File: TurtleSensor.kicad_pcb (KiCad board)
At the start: 2 copper layers, 40 x 40 mm, 14 parts, among them IC1 ATMEGA328P-A, J2 FTDIConnector, U1 SI7021, U2 M24512

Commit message: rotated capacitor to be parallel
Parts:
- moved 22pF2 0.90 mm to (135.0, 103.0), turned to 90 degrees
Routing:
- net Net-(22pF2-Pad2): track 10.5 -> 8.98 mm
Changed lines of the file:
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@@
     (thickness 1.6)
     (drawings 4)
-    (tracks 168)
+    (tracks 167)
     (zones 0)
     (modules 14)
@@
   )
   (module Capacitors_SMD:C_0805_HandSoldering placed (layer F.Cu)
-    (at 134.25 103.5 135)
+    (at 135 103 90)
     (descr "Capacitor SMD 0805, hand soldering")
     (tags "capacitor 0805")
     (attr smd)
-    (fp_text reference 22pF2 (at 0 -2.1 135) (layer F.SilkS)
-      (effects (font (size 1 1) (thickness 0.15)))
-    )
-    (fp_text value C (at 0 2.1 135) (layer F.Fab)
+    (fp_text reference 22pF2 (at 0 -2.1 90) (layer F.SilkS)
+      (effects (font (size 1 1) (thickness 0.15)))
+    )
+    (fp_text value C (at 0 2.1 90) (layer F.Fab)
       (effects (font (size 1 1) (thickness 0.15)))
     )
@@
     (fp_line (start 0.5 -0.85) (end -0.5 -0.85) (layer F.SilkS) (width 0.15))
     (fp_line (start -0.5 0.85) (end 0.5 0.85) (layer F.SilkS) (width 0.15))
-    (pad 1 smd rect (at -1.25 0 135) (size 1.5 1.25) (layers F.Cu F.Paste F.Mask)
-      (net 3 GND))
-    (pad 2 smd rect (at 1.25 0 135) (size 1.5 1.25) (layers F.Cu F.Paste F.Mask)
+    (pad 1 smd rect (at -1.25 0 90) (size 1.5 1.25) (layers F.Cu F.Paste F.Mask)
+      (net 3 GND))
+    (pad 2 smd rect (at 1.25 0 90) (size 1.5 1.25) (layers F.Cu F.Paste F.Mask)
       (net 2 "Net-(22pF2-Pad2)"))
     (model Capacitors_SMD.3dshapes/C_0805_HandSoldering.wrl
@@
     (effects (font (size 1.5 1.5) (thickness 0.3)))
   )
-  (segment (start 133 91.75) (end 133 93.65) (width 0.4) (layer F.Cu) (net 1) (status 400000))
-  (segment (start 133 93.65) (end 135 95.65) (width 0.4) (layer F.Cu) (net 1) (status 800000))
-  (segment (start 140.25 96.75) (end 136.75 96.75) (width 0.4) (layer F.Cu) (net 1) (status 400000))
-  (segment (start 136.75 96.75) (end 135.65 95.65) (width 0.4) (layer F.Cu) (net 1) (status 800000))
-  (segment (start 135.65 95.65) (end 135 95.65) (width 0.4) (layer F.Cu) (net 1) (status C00000))
-  (segment (start 135 95.65) (end 135 95) (width 0.3) (layer F.Cu) (net 1) (status C00000))
+  (segment (start 133 91.75) (end 133 93.65) (width 0.4) (layer F.Cu) (net 1))
+  (segment (start 133 93.65) (end 135 95.65) (width 0.4) (layer F.Cu) (net 1))
+  (segment (start 140.25 96.75) (end 136.75 96.75) (width 0.4) (layer F.Cu) (net 1))
+  (segment (start 136.75 96.75) (end 135.65 95.65) (width 0.4) (layer F.Cu) (net 1))
+  (segment (start 135.65 95.65) (end 135 95.65) (width 0.4) (layer F.Cu) (net 1))
+  (segment (start 135 95.65) (end 135 95) (width 0.3) (layer F.Cu) (net 1))
   (segment (start 133 92) (end 133 91.75) (width 0.25) (layer F.Cu) (net 1))
-  (segment (start 135 98.35) (end 135 100.982234) (width 0.4) (layer F.Cu) (net 2) (status 400000))
-  (segment (start 135 100.982234) (end 133.366117 102.616117) (width 0.4) (layer F.Cu) (net 2) (status 800000))
-  (segment (start 140.25 97.55) (end 137.45 97.55) (width 0.4) (layer F.Cu) (net 2) (status 400000))
-  (segment (start 136.65 98.35) (end 135 98.35) (width 0.4) (layer F.Cu) (net 2) (status 800000))
+  (segment (start 135 98.35) (end 135 101.75) (width 0.4) (layer F.Cu) (net 2) (status C00000))
+  (segment (start 140.25 97.55) (end 137.45 97.55) (width 0.4) (layer F.Cu) (net 2))
+  (segment (start 136.65 98.35) (end 135 98.35) (width 0.4) (layer F.Cu) (net 2))
   (segment (start 137.45 97.55) (end 136.65 98.35) (width 0.4) (layer F.Cu) (net 2))
   (segment (start 136.75 89) (end 137.5 89) (width 0.5) (layer F.Cu) (net 3))
@@
   (segment (start 145 79) (end 142 79) (width 0.5) (layer F.Cu) (net 11))
   (segment (start 145.84 79.84) (end 145 79) (width 0.5) (layer F.Cu) (net 11))
-  (segment (start 148.75 97.55) (end 148.75 101.25) (width 0.4) (layer F.Cu) (net 12) (status 400000))
-  (segment (start 146.79902 103.20098) (end 145.5 103.20098) (width 0.4) (layer F.Cu) (net 12) (status 800000))
+  (segment (start 148.75 97.55) (end 148.75 101.25) (width 0.4) (layer F.Cu) (net 12))
+  (segment (start 146.79902 103.20098) (end 145.5 103.20098) (width 0.4) (layer F.Cu) (net 12))
   (segment (start 148.75 101.25) (end 146.79902 103.20098) (width 0.4) (layer F.Cu) (net 12))
 )

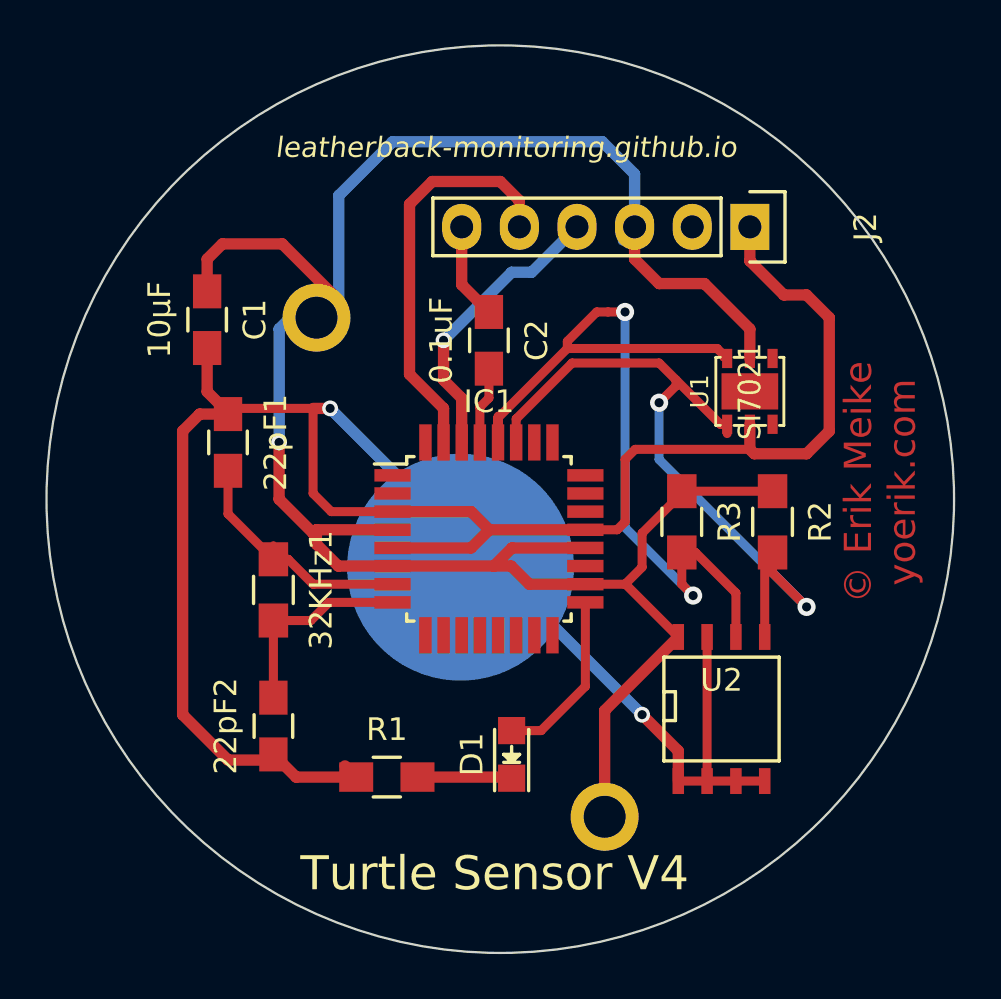
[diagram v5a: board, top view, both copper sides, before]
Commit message: rerouted power
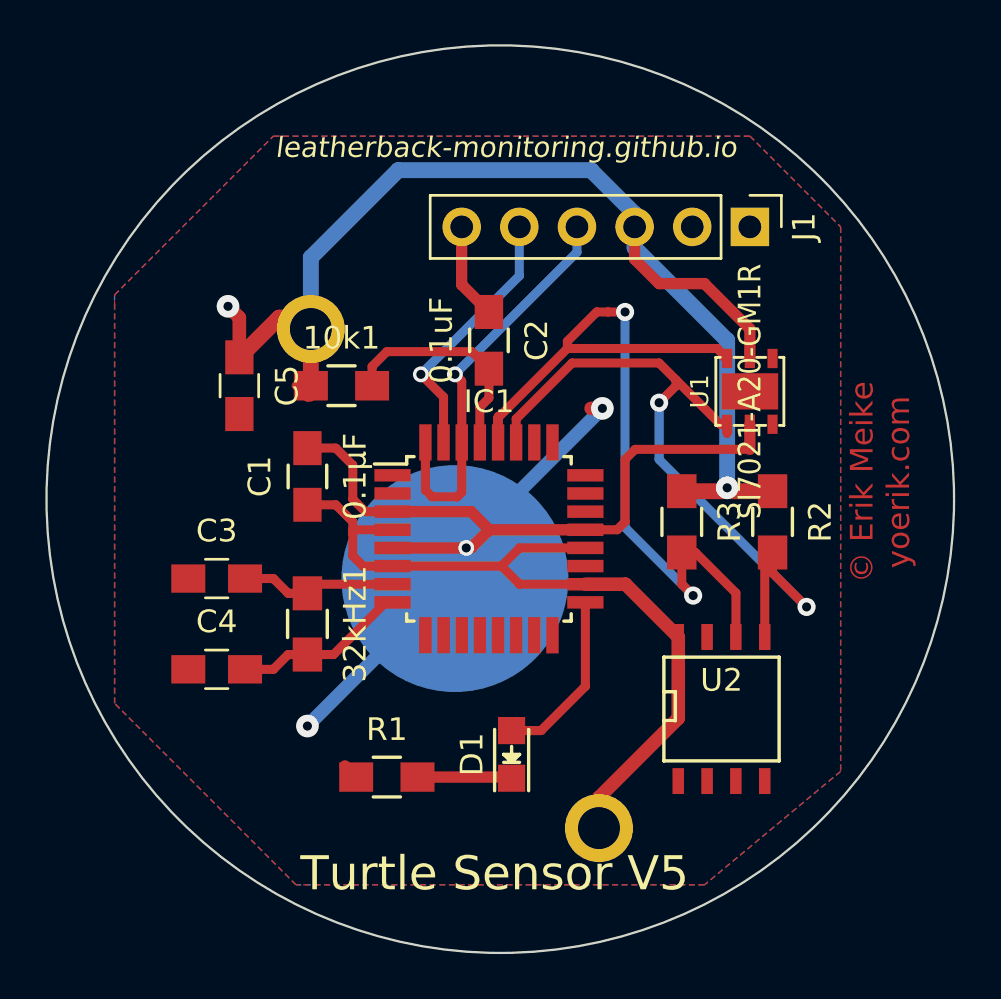
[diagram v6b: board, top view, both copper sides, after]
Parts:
- removed 22pF1, 22pF2: C, Capacitors_SMD:C_0805_HandSoldering
- removed 32KHz1: Crystal, Resistors_SMD:R_0805_HandSoldering
- removed J2: FTDIConnector, Pin_Headers:Pin_Header_Straight_1x06
- added 10k1: 10k, Resistors_SMD:R_0805_HandSoldering, F.Cu at (138.0, 88.0)
- added 32kHz1: TXC 9HT11-32.768KDZF-T, Resistors_SMD:R_0805_HandSoldering, F.Cu at (136.5, 98.5)
- added C3: 12.5pF, Capacitors_SMD:C_0805_HandSoldering, F.Cu at (132.5, 96.5)
- added C4: 12.5pF, Capacitors_SMD:C_0805_HandSoldering, F.Cu at (132.5, 100.5)
- added C5: 10µF, Capacitors_SMD:C_0805_HandSoldering, F.Cu at (133.5, 88.0)
- added J1: FTDIConnector, Pin_Headers:Pin_Header_Straight_1x06_Pitch2.54mm, F.Cu at (156.0, 81.0)
- BT1: value Battery -> 534-3039
- C1: value 10µF -> 0.1µF
- D1: value LED -> 5988110107F
- IC1: value ATMEGA328P-A -> ATMEGA328PB-A
- R1: value 470 -> 33Ω
- R2, R3: value 4k -> 4k7
- U1: value SI7021 -> SI7021-A20-GM1R
- U2: value M24512 -> M24M01-RMN6TP
- moved C1 8.20 mm to (136.5, 92.0), turned to 90 degrees
- moved BT1 0.56 mm to (143.0, 96.5)
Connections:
- IC1 pad 1: (no net) -> Net-(IC1-Pad1)
- IC1 pad 10: (no net) -> Net-(IC1-Pad10)
- IC1 pad 11: (no net) -> Net-(IC1-Pad11)
- IC1 pad 12: (no net) -> Net-(IC1-Pad12)
- IC1 pad 13: (no net) -> Net-(IC1-Pad13)
- IC1 pad 14: (no net) -> /~SS
- IC1 pad 15: (no net) -> /MOSI
- IC1 pad 16: (no net) -> /MISO
- IC1 pad 19: (no net) -> Net-(IC1-Pad19)
- IC1 pad 2: (no net) -> Net-(IC1-Pad2)
- IC1 pad 22: (no net) -> Net-(IC1-Pad22)
- IC1 pad 23: (no net) -> Net-(IC1-Pad23)
- IC1 pad 24: (no net) -> Net-(IC1-Pad24)
- IC1 pad 25: (no net) -> Net-(IC1-Pad25)
- IC1 pad 26: (no net) -> Net-(IC1-Pad26)
- IC1 pad 32: (no net) -> /RX
- IC1 pad 9: (no net) -> Net-(IC1-Pad9)
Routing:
- net GND: track 113.5 -> 50.8 mm, vias 2 -> 3
- net /~RST: track 3.42 -> 10.00 mm
- net /TX: track 17.9 -> 11.7 mm, vias 0 -> 1
- net /RX: track 12.8 -> 18.0 mm
- net Net-(32kHz1-Pad1): track 11.3 -> 6.93 mm
- net +BATT: track 96.5 -> 93.2 mm, vias 1 -> 2
- net Net-(32kHz1-Pad2): track 8.98 -> 7.72 mm
- added copper zone on B.Cu, net +BATT
- added copper zone on F.Cu, net GND
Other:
- net class Power: trace_width 0.7 -> 0.6
- board text added: "Turtle Sensor V5"
- board text removed: "Turtle Sensor V4"

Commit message: rev5
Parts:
- moved R1 2.30 mm to (139.5, 103.0)
- moved C5 2.00 mm to (133.5, 90.0)
- moved D1 1.60 mm to (144.5, 103.0), turned to 0 degrees
- moved C1 1.12 mm to (137.0, 93.0)
- moved 32kHz1 0.50 mm to (137.0, 98.5)
- moved C3 0.50 mm to (133.0, 96.5)
- moved C4 0.50 mm to (133.0, 100.5)
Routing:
- net +BATT: track 93.2 -> 64.3 mm
- net GND: track 50.8 -> 44.1 mm
- net Net-(D1-Pad1): track 4.24 -> 2.60 mm
